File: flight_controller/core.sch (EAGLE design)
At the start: 108 parts, among them J1 MOLEX-2POS, J13 MOLEX-3POS, J14 MOLEX-3POS, J15 MOLEX-4POS, J16 MOLEX-3POS, J17 MOLEX-3POS, J18 MOLEX-4POS, J19 MOLEX-3POS, J2 MOLEX-2POS, J20 MOLEX-4POS, J3 MOLEX-2POS, J4 MOLEX-2POS, J5 MOLEX-2POS, J6 MOLEX-2POS, J7 MOLEX-2POS, J8 MOLEX-2POS, J9 MOLEX-2POS, Q1 MMBT2222A, Q14 MMBT2222A, Q15 MMBT2222A, Q16 MMBT2222A, Q17 MMBT2222A, Q2 200mA/50V, Q3 MMBT2222A, Q4 MMBT2222A, Q5 200mA/50V, Q6 200mA/50V, Q9 MMBT2222A, U1 MPU-6000QFN-24, U2 MEAS-MS5611, U3 USD-SOCKETNEW, U4 STM32F405, U5 MIC5219 3.3V

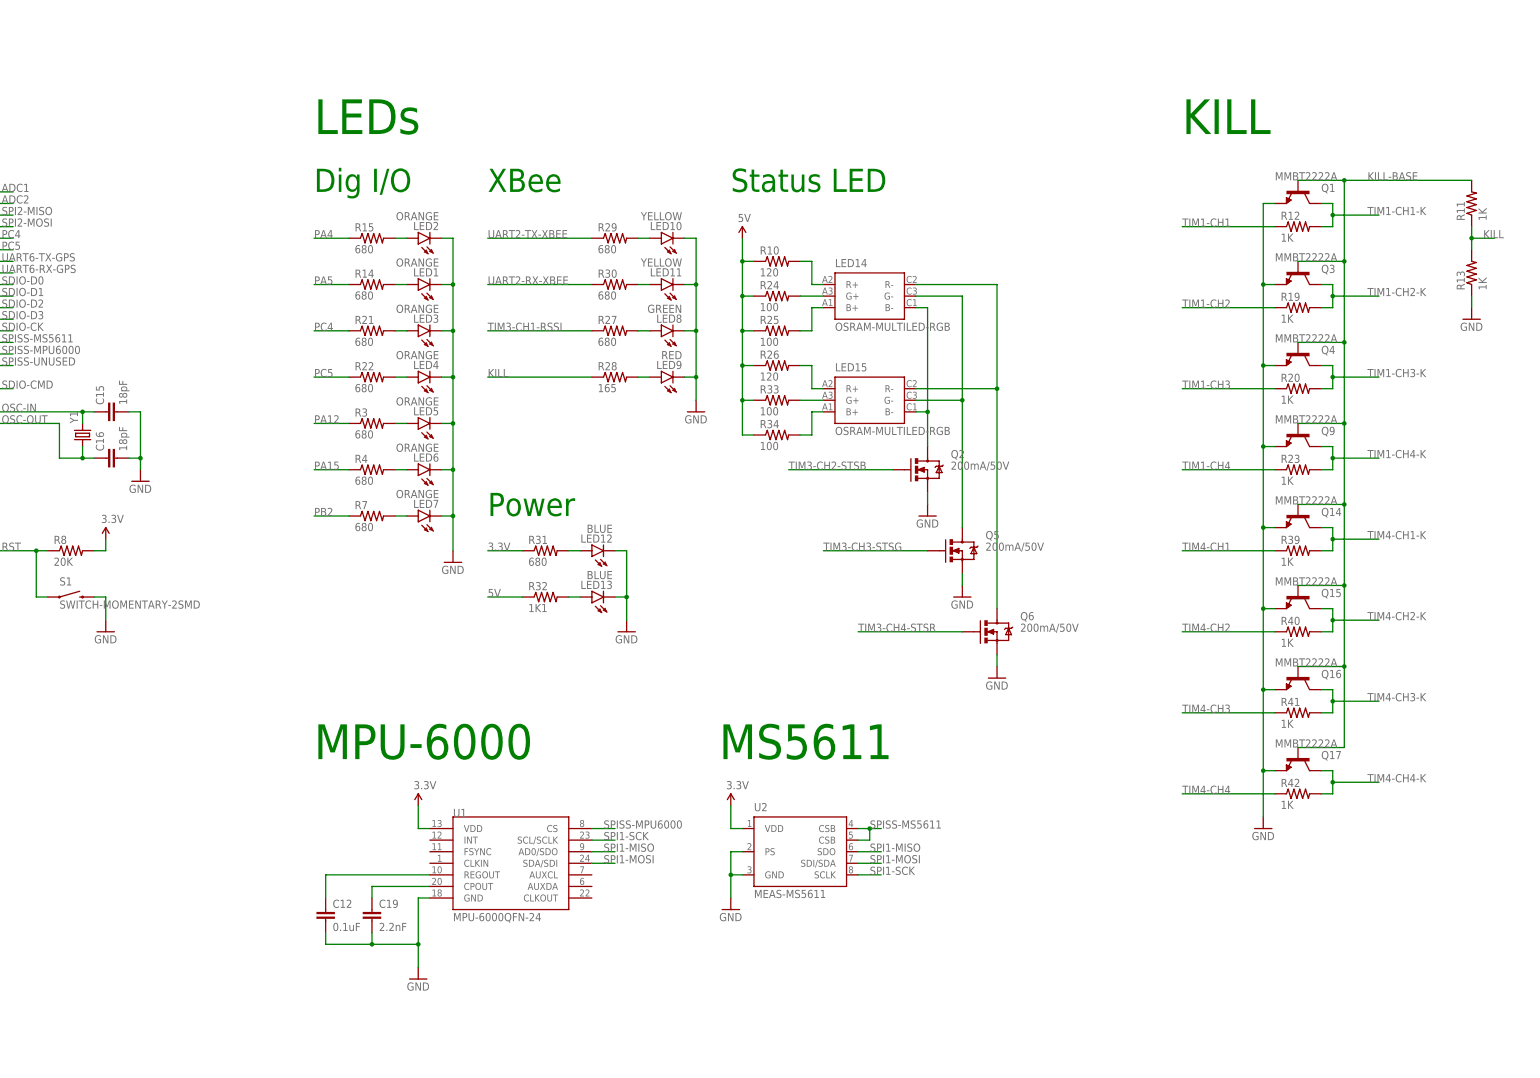
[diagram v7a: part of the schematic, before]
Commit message: Change kill BJTs to dual N-ch MOSFETs.
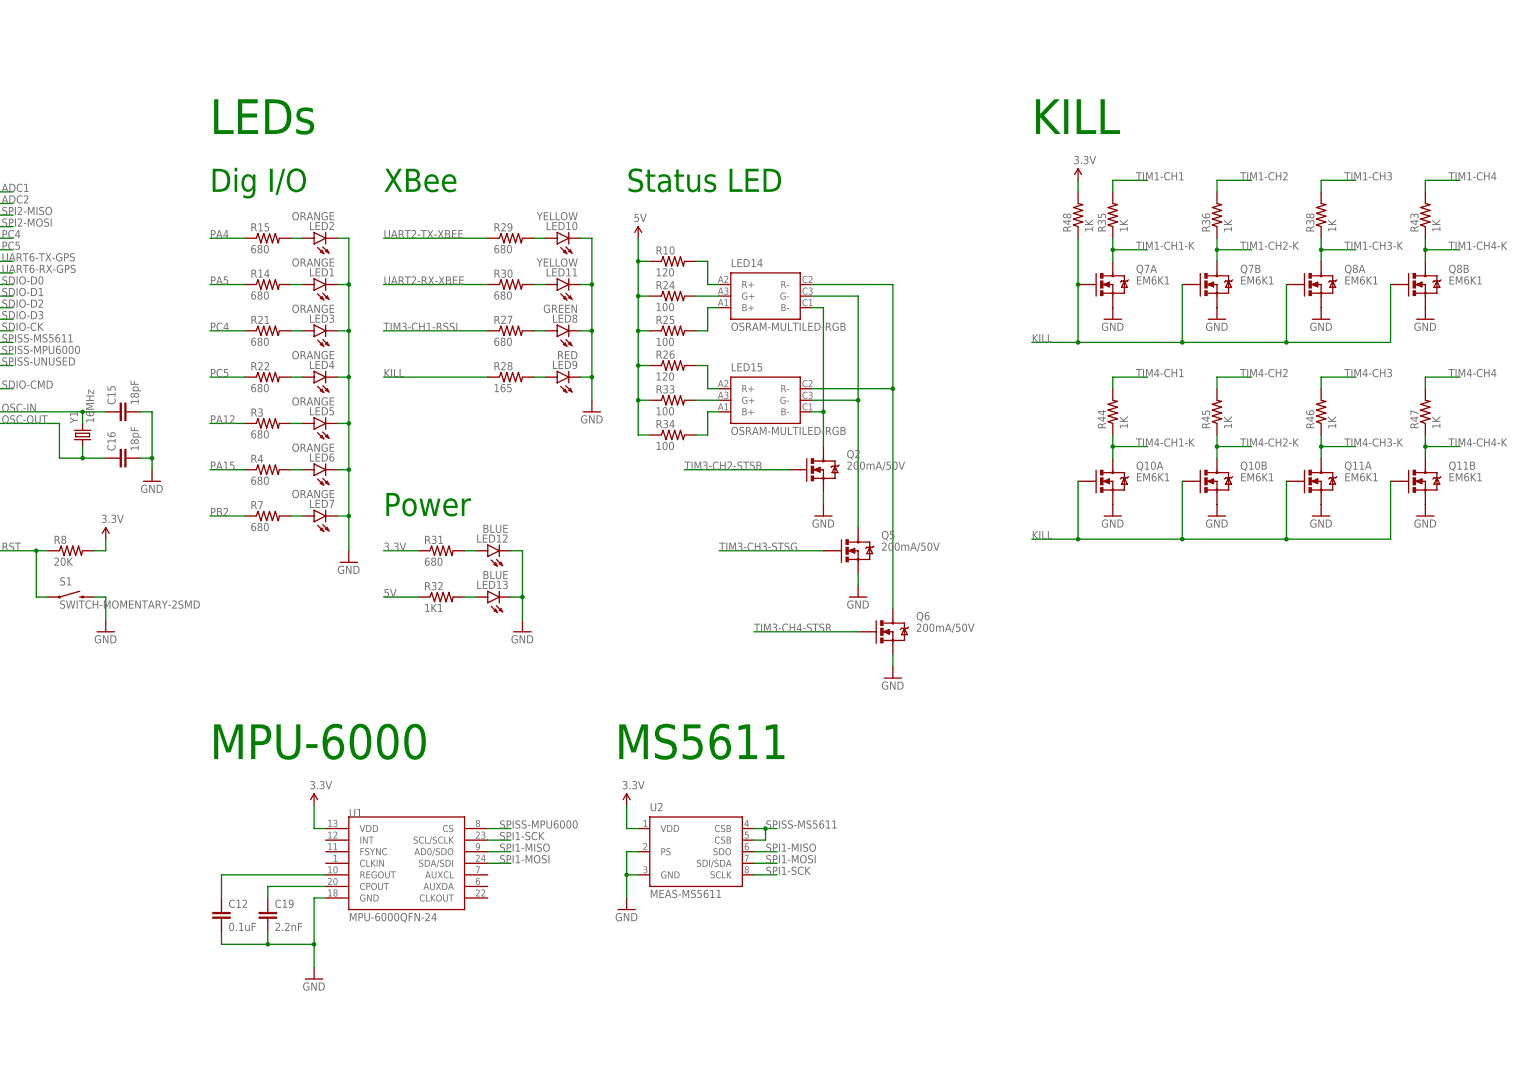
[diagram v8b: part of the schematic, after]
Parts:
- removed Q1, Q14, Q15, Q16, Q17, Q3, Q4, Q9: MMBT2222A, SparkFun-DiscreteSemi:TRANSISTOR_NPNMMBT2222A
- removed R11, R12, R13, R19, R20, R23, R39, R40, R41, R42: 1K, SparkFun:RESISTOR0603-RES
- added Q10, Q11, Q7, Q8: EM6K1, OSURC_DiscreteSemi:MOSFET-NCHANNEL-DUALEM6K1
- added R35, R36, R38, R43, R44, R45, R46, R47, R48: 1K, SparkFun:RESISTOR0603-RES
- J1: value MOLEX-2POS -> M02; device OSURC_Connectors:MOLEX-2POS -> OSURC_Connectors:M02
- J17: value MOLEX-3POS -> M03; device OSURC_Connectors:MOLEX-3POS -> OSURC_Connectors:M03
- J18: value MOLEX-4POS -> M04; device OSURC_Connectors:MOLEX-4POS -> OSURC_Connectors:M04
- LED15: device aerial:OSRAM-MULTILED-RGB -> OSURC_LED:OSRAM-MULTILED-RGB
- Y1: value (none) -> 16MHz
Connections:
- removed net KILL-BASE: Q1.B, Q14.B, Q15.B, Q16.B, Q17.B, Q3.B, Q4.B, Q9.B, R11.2
- new net KILL1: Q10A.G, Q10B.G, Q11A.G, Q11B.G
- net 3.3V: now also R48.2
- net GND: now also Q10A.S, Q10B.S, Q11A.S, Q11B.S, Q7A.S, Q7B.S, Q8A.S, Q8B.S; no longer Q1.E, Q14.E, Q15.E, Q16.E, Q17.E, Q3.E, Q4.E, Q9.E, R13.1
- net KILL: now also Q7A.G, Q7B.G, Q8A.G, Q8B.G, R48.1; no longer R11.1, R13.2
- net TIM1-CH1: now also R35.2; no longer R12.1
- net TIM1-CH1-K: now also Q7A.D, R35.1; no longer Q1.C, R12.2
- net TIM1-CH2: now also R36.2; no longer R19.1
- net TIM1-CH2-K: now also Q7B.D, R36.1; no longer Q3.C, R19.2
- net TIM1-CH3: now also R38.2; no longer R20.1
- net TIM1-CH3-K: now also Q8A.D, R38.1; no longer Q4.C, R20.2
- net TIM1-CH4: now also R43.2; no longer R23.1
- net TIM1-CH4-K: now also Q8B.D, R43.1; no longer Q9.C, R23.2
- net TIM4-CH1: now also R44.2; no longer R39.1
- net TIM4-CH1-K: now also Q10A.D, R44.1; no longer Q14.C, R39.2
- net TIM4-CH2: now also R45.2; no longer R40.1
- net TIM4-CH2-K: now also Q10B.D, R45.1; no longer Q15.C, R40.2
- net TIM4-CH3: now also R46.2; no longer R41.1
- net TIM4-CH3-K: now also Q11A.D, R46.1; no longer Q16.C, R41.2
- net TIM4-CH4: now also R47.2; no longer R42.1
- net TIM4-CH4-K: now also Q11B.D, R47.1; no longer Q17.C, R42.2
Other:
- note added: "1K pullup on KILL keeps these N-ch MOSFETS on, pulling TIM1 and TIM4 channels down, until the XBee deasserts KILL."
- moved on the sheet: C12, C15, C16, C19, LED1, LED10, LED11, LED12, LED13, LED14, LED15, LED2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
